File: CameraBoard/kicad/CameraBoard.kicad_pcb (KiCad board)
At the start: 2 copper layers, 101.6 x 76.2 mm, 100 parts, among them Q1 SI7465DP-T1-E3, Q2 BVSS123LT1G, Q3 BSS84, U1 MP26124GR-Z, U2 TPS63070, U3 LM2678SD-12/NOPB, U4 TS5A3159ADBVR, U5 ICM7242IBAZ-SMD, U6 H11F1SR2M, U7 H11F1SR2M, U8 SN74LVC1G17DCKR

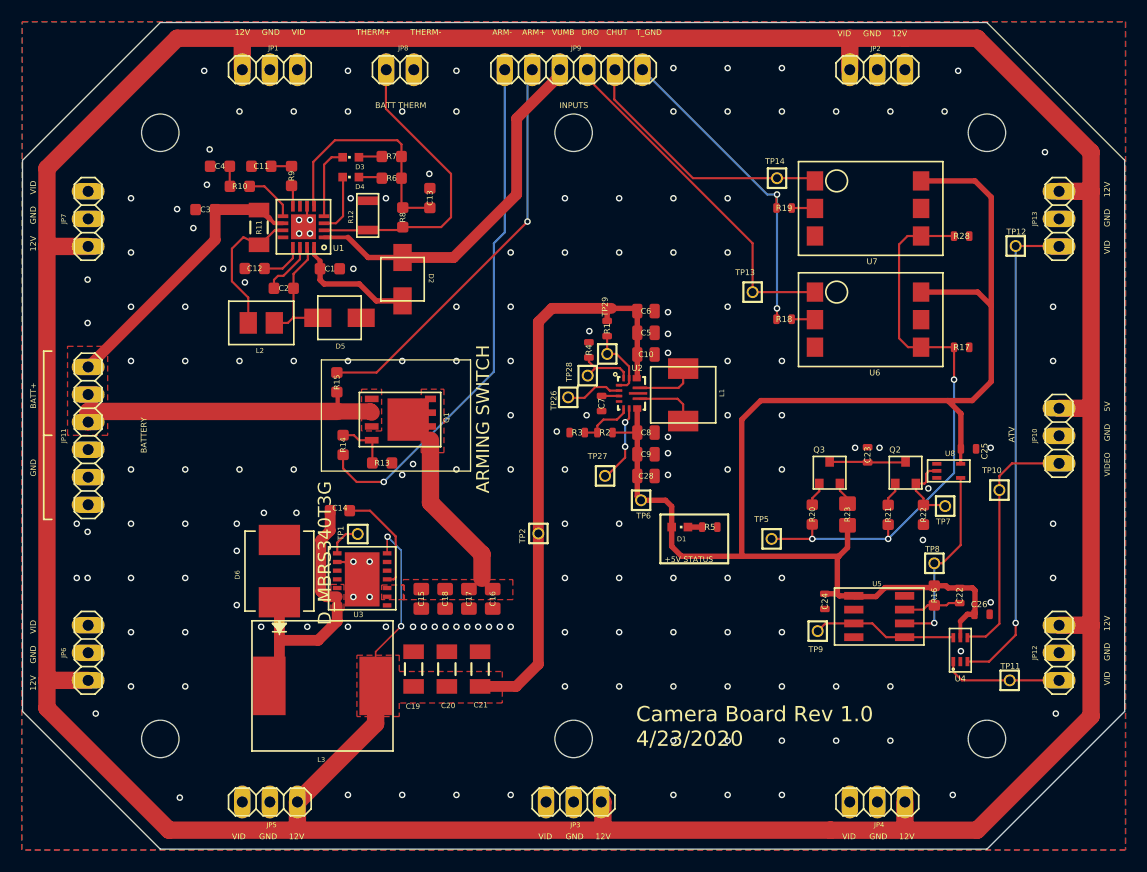
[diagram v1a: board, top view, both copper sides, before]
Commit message: PCB made from new schematic
Made the PCB. There are a few weird errors.
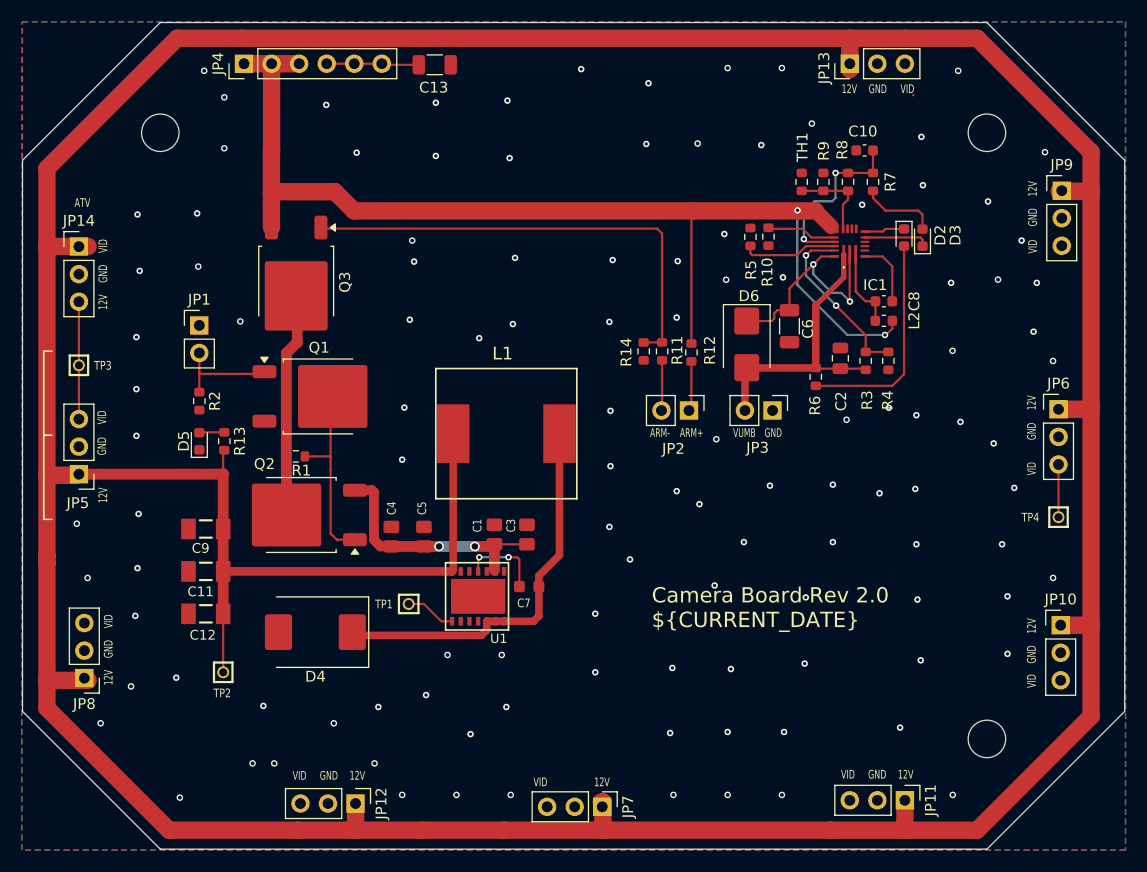
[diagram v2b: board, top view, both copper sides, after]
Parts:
- removed C14: 10n, CameraBoard:.0603-A-NOSILK
- removed C15, C16, C17, C18: 10u, CameraBoard:.0805-B-NOSILK
- removed C19, C20, C21: 47u, CameraBoard:1206-A
- removed C22: 1u, CameraBoard:.0603-C-NOSILK
- removed C23: 20u, CameraBoard:.0603-C-NOSILK
- removed C24, C25, C26: 100n, CameraBoard:.0603-C-NOSILK
- removed C28: 22u, CameraBoard:.0805-C-NOSILK
- removed D1: GRN, CameraBoard:CHIPLED_0603_259
- removed L3: 784770220, CameraBoard:784770220
- removed R15, R22: 1k, CameraBoard:.0603-A-NOSILK
- removed R16: 237k, CameraBoard:.0603-A-NOSILK
- removed R17, R28: 10k, CameraBoard:.0603-C-NOSILK
- removed R18, R19: 60.4, CameraBoard:.0603-C-NOSILK
- removed R20, R21: 10k, CameraBoard:.0603-A-NOSILK
- removed R23: 10, CameraBoard:.0805-A-NOSILK
- removed TP10, TP11, TP12, TP13, TP14, TP26, TP27, TP28, TP29, TP5, TP6, TP7, TP8, TP9: TEST-POINT, CameraBoard:2MM-TEST-POINT
- removed U2: TPS63070, CameraBoard:TPS63070X
- removed U3: LM2678SD-12/NOPB, CameraBoard:LM2678SD-12_NOPB
- removed U4: TS5A3159ADBVR, CameraBoard:TS5A3159ADBVR
- removed U5: ICM7242IBAZ-SMD, CameraBoard:ICM7242IBAZ-SMD
- removed U6, U7: H11F1SR2M, CameraBoard:H11F1SR2M
- removed U8: SN74LVC1G17DCKR, CameraBoard:SN74LVC1G17DCKR
- added IC1: MP2659GQ-0000-Z, psas-footprints:MP2659GQ0000Z, F.Cu at (173.9, 87.3)
- added JP14: PINHD-1X3, Connector_PinHeader_2.54mm:PinHeader_1x03_P2.54mm_Vertical, F.Cu at (102.9, 87.6)
- added TH1: 10k, Resistor_SMD:R_0603_1608Metric, F.Cu at (169.5, 81.6)
- added TP3: Test-Point, CameraBoard:2MM-TEST-POINT, F.Cu at (102.9, 98.5)
- added TP4: Test-Point, CameraBoard:2MM-TEST-POINT, F.Cu at (193.2, 112.5)
- C1: value 4.7u -> 10u; footprint CameraBoard:.0603-A-NOSILK -> CameraBoard:.0805-B-NOSILK
- C10: value 10u -> 1u; footprint CameraBoard:.0805-C-NOSILK -> Capacitor_SMD:C_0603_1608Metric
- C11: value 2.2n -> 47u; footprint CameraBoard:.0603-A-NOSILK -> CameraBoard:1206-A
- C12: value 100n -> 47u; footprint CameraBoard:.0603-A-NOSILK -> CameraBoard:1206-A
- C13: value 1u -> 10u; footprint CameraBoard:.0603-A-NOSILK -> Capacitor_SMD:C_1206_3216Metric
- C2: value 100n -> 1u; footprint CameraBoard:.0603-A-NOSILK -> Capacitor_SMD:C_0805_2012Metric
- C3: footprint CameraBoard:.0603-A-NOSILK -> CameraBoard:.0805-B-NOSILK
- C4: value 4.7n -> 10u; footprint CameraBoard:.0603-A-NOSILK -> CameraBoard:.0805-B-NOSILK
- C5: footprint CameraBoard:.0805-C-NOSILK -> CameraBoard:.0805-B-NOSILK
- C6: value 10u -> 2.2u; footprint CameraBoard:.0805-C-NOSILK -> Capacitor_SMD:C_1206_3216Metric
- C7: value 100n -> 10n; footprint CameraBoard:.0603-C-NOSILK -> CameraBoard:.0603-A-NOSILK
- C8: value 22u -> 100n; footprint CameraBoard:.0805-C-NOSILK -> Capacitor_SMD:C_0603_1608Metric
- C9: value 22u -> 47u; footprint CameraBoard:.0805-C-NOSILK -> CameraBoard:1206-A
- D2, D5: value S2MA-13-F -> LED_Small_Filled; footprint CameraBoard:S2MA-13-F -> LED_SMD:LED_0603_1608Metric
- D3: value SML-D12U1WT86 -> LED_Small_Filled; footprint CameraBoard:CHIPLED_0603_259 -> LED_SMD:LED_0603_1608Metric
- D4: value SML-D12U1WT86 -> D_MBRS340T3G; footprint CameraBoard:CHIPLED_0603_259 -> Diode_SMD:D_SMC
- D6: value D_MBRS340T3G -> B240; footprint CameraBoard:SMC -> Diode_SMD:D_SMB
- JP1, JP2, JP3: value PINHD-1X3 -> ~; footprint CameraBoard:1X03_325 -> Connector_PinHeader_2.54mm:PinHeader_1x02_P2.54mm_Vertical
- JP10, JP12, JP13, JP5, JP6, JP7: footprint CameraBoard:1X03_325 -> Connector_PinHeader_2.54mm:PinHeader_1x03_P2.54mm_Vertical
- JP11, JP9: value PINHD-1X6 -> PINHD-1X3; footprint CameraBoard:1X06_325 -> Connector_PinHeader_2.54mm:PinHeader_1x03_P2.54mm_Vertical
- JP4: value PINHD-1X3 -> PINHD-1X6; footprint CameraBoard:1X03_325 -> Connector_PinHeader_2.54mm:PinHeader_1x06_P2.54mm_Vertical
- JP8: value PINHD-1X2 -> PINHD-1X3; footprint CameraBoard:1X02_325 -> Connector_PinHeader_2.54mm:PinHeader_1x03_P2.54mm_Vertical
- L1: value 1.5uH -> 784770220; footprint CameraBoard:IHLP2020CZER1R5M11 -> CameraBoard:784770220
- L2: value 10uH -> 10uh; footprint CameraBoard:1239AS-H-100M=P2 -> Inductor_SMD:L_0603_1608Metric
- Q1: value SI7465DP-T1-E3 -> SUD08P06-155L; footprint CameraBoard:SI7465DP-T1-E3CT-ND -> Package_TO_SOT_SMD:TO-252-2
- Q2: value BVSS123LT1G -> SUD08P06-155L; footprint CameraBoard:BVSS123LT1G -> Package_TO_SOT_SMD:TO-252-2
- Q3: value BSS84 -> SUD08P06-155L; footprint CameraBoard:BSS84 -> Package_TO_SOT_SMD:TO-252-2
- R1, R4: footprint CameraBoard:.0603-C-NOSILK -> Resistor_SMD:R_0603_1608Metric
- R10: value 750 -> 38.4k; footprint CameraBoard:.0603-A-NOSILK -> Resistor_SMD:R_0603_1608Metric
- R11: value 200m -> 1k; footprint CameraBoard:1206-A -> Resistor_SMD:R_0603_1608Metric
- R12: value 10K -> 1k; footprint CameraBoard:NHQ103B375T10 -> Resistor_SMD:R_0603_1608Metric
- R13: value 150k -> 3.3k; footprint CameraBoard:.0603-A-NOSILK -> Resistor_SMD:R_0603_1608Metric
- R14: value 1k -> 150k; footprint CameraBoard:.0603-A-NOSILK -> Resistor_SMD:R_0603_1608Metric
- R2: value 680k -> 10k; footprint CameraBoard:.0603-C-NOSILK -> Resistor_SMD:R_0603_1608Metric
- R3: value 130k -> 133k; footprint CameraBoard:.0603-C-NOSILK -> Resistor_SMD:R_0603_1608Metric
- R5: value 400 -> 33k; footprint CameraBoard:.0603-C-NOSILK -> Resistor_SMD:R_0603_1608Metric
- R6: value 230 -> 10k; footprint CameraBoard:.0603-A-NOSILK -> Resistor_SMD:R_0603_1608Metric
- R7: value 230 -> 2k; footprint CameraBoard:.0603-A-NOSILK -> Resistor_SMD:R_0603_1608Metric
- R8: value 10k -> 2.26k; footprint CameraBoard:.0603-A-NOSILK -> Resistor_SMD:R_0603_1608Metric
- R9: value 42.5k -> 6.95k; footprint CameraBoard:.0603-A-NOSILK -> Resistor_SMD:R_0603_1608Metric
- TP1, TP2: value TEST-POINT -> Test-Point
- U1: value MP26124GR-Z -> LM2678SD-12/NOPB; footprint CameraBoard:MP26124GR-Z -> CameraBoard:LM2678SD-12_NOPB
- moved JP6 92.2 mm to (193.2, 102.6), turned to 0 degrees
- moved JP4 89.7 mm to (118.1, 70.7), turned to 90 degrees
- moved JP11 82.4 mm to (179.0, 138.6)
- moved JP7 72.0 mm to (151.1, 139.2), turned to -90 degrees
- moved JP12 66.3 mm to (128.4, 138.9)
- moved JP8 63.2 mm to (103.4, 127.3), turned to 180 degrees
- moved L2 57.4 mm to (177.1, 94.4), turned to 0 degrees
- moved Q2 55.9 mm to (123.3, 112.3), turned to 180 degrees
- moved D3 53.2 mm to (180.7, 86.7)
- moved Q3 52.6 mm to (122.9, 90.8), turned to -90 degrees
- moved C2 51.7 mm to (173.1, 97.9), turned to 90 degrees
- moved R9 49.0 mm to (171.5, 81.6)
- moved R10 48.9 mm to (166.5, 86.6), turned to -90 degrees
- moved D6 47.9 mm to (164.5, 96.6), turned to -90 degrees
- moved D2 46.4 mm to (179.0, 86.7)
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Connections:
- C1 pad 1: Net-(D2--) -> Net-(Q2-S)
- C10 pad 1: +12V -> VCC
- C11 pad 1: Net-(C11-Pad1) -> +12V
- C12 pad 1: Net-(C12-Pad1) -> +12V
- C13 pad 1: Net-(C13-Pad1) -> Net-(JP4-Pin_4)
- C2 pad 1: Net-(D5--) -> /VUMB
- C2 pad 2: Net-(C2-Pad2) -> GND
- C3 pad 1: /CameraBoard_1/BATT+ -> Net-(Q2-S)
- C4 pad 1: Net-(C4-Pad1) -> Net-(Q2-S)
- C5 pad 1: +12V -> Net-(Q2-S)
- C6 pad 1: +12V -> GND
- C6 pad 2: GND -> Net-(D6-K)
- C7 pad 1: Net-(U2-VAUX) -> /SOUT
- C7 pad 2: GND -> Net-(U1-CB)
- C8 pad 1: +5V -> Net-(IC1-BST)
- C8 pad 2: GND -> Net-(IC1-SW)
- C9 pad 1: +5V -> +12V
- D6 pad 1: /CameraBoard_1/SOUT -> Net-(D6-K)
- D6 pad 2: GND -> /VUMB
- JP1 pad 1: +12V -> GND
- JP1 pad 2: GND -> Net-(JP1-Pin_2)
- JP10 pad 3: Net-(U4-COM) -> unconnected-(JP10-Pin_3-Pad3)
- JP11 pad 1: /CameraBoard_1/BATT+ -> +12V
- JP11 pad 2: /CameraBoard_1/BATT+ -> GND
- JP11 pad 3: /CameraBoard_1/BATT+ -> unconnected-(JP11-Pin_3-Pad3)
- JP12 pad 3: /CameraBoard_2/CAM_DOWN -> unconnected-(JP12-Pin_3-Pad3)
- JP13 pad 3: /CameraBoard_2/CAM_UP -> unconnected-(JP13-Pin_3-Pad3)
- JP2 pad 1: +12V -> /ARM-OUT
- JP2 pad 2: GND -> /ARM-IN
- JP3 pad 1: +12V -> GND
- JP3 pad 2: GND -> /VUMB
- JP4 pad 1: +12V -> /BATT+
- JP4 pad 2: GND -> /BATT+
- JP4 pad 3: unconnected-(JP4-Pad3) -> /BATT+
- JP5 pad 3: unconnected-(JP5-Pad3) -> /CAM_DOWN
- JP6 pad 3: unconnected-(JP6-Pad3) -> /CAM_UP
- JP8 pad 1: Net-(R12-P$1) -> +12V
- JP9 pad 1: T_GND -> +12V
- JP9 pad 2: CHUTE -> GND
- JP9 pad 3: DROGUE -> unconnected-(JP9-Pin_3-Pad3)
- Q2 pad 1: Net-(Q2-G) -> Net-(Q1-D)
- Q2 pad 2: Net-(Q2-S) -> VBATT
- Q2 pad 3: Net-(Q2-D) -> Net-(Q2-S)
- Q3 pad 2: Net-(Q3-S) -> VBATT
- Q3 pad 3: Net-(Q2-D) -> /BATT+
- R1 pad 1: Net-(U2-EN) -> VBATT
- R1 pad 2: +12V -> Net-(Q1-D)
- R10 pad 1: Net-(R10-Pad1) -> Net-(IC1-ISET)
- R10 pad 2: Net-(C4-Pad1) -> GND
- R11 pad 1: Net-(L2-P$2) -> /ARM-IN
- R11 pad 2: /CameraBoard_1/BATT+ -> Net-(Q3-G)
- R13 pad 1: GND -> Net-(D5-A)
- R13 pad 2: Net-(Q1-PadG) -> +12V
- R14 pad 1: Net-(Q1-PadG) -> Net-(Q3-G)
- R14 pad 2: /CameraBoard_1/ARM-IN -> GND
- R2 pad 1: Net-(U2-FB) -> Net-(JP1-Pin_2)
- R2 pad 2: +5V -> GND
- R3 pad 1: GND -> Net-(IC1-VDPM)
- R3 pad 2: Net-(U2-FB) -> /VUMB
- R4 pad 2: Net-(U2-VSEL) -> Net-(IC1-VDPM)
- R6 pad 1: Net-(D4-PadA) -> /VUMB
- R6 pad 2: Net-(C13-Pad1) -> Net-(D2-A)
- R7 pad 1: Net-(D3-PadA) -> VCC
- R7 pad 2: Net-(C13-Pad1) -> Net-(D3-A)
- R8 pad 1: Net-(R12-P$1) -> VCC
- R8 pad 2: Net-(C13-Pad1) -> Net-(IC1-NTC)
- R9 pad 1: Net-(R9-Pad1) -> Net-(IC1-NTC)
- R9 pad 2: Net-(C11-Pad1) -> GND
- TP1 pad 1: Net-(U3-ON) -> Net-(U1-ON)
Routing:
- net +5V: track 134.4 -> 0.00 mm
- net /BATT+: track 0.00 -> 103.8 mm, vias 0 -> 2
- net /CameraBoard_1/BATT+: track 55.1 -> 0.00 mm
- net /CameraBoard_2/TIMERPULSE: track 53.0 -> 0.00 mm, vias 3 -> 0
- net /CameraBoard_1/ARM-IN: track 48.1 -> 0.00 mm, vias 1 -> 0
- net /CameraBoard_2/CAM_UP: track 45.3 -> 0.00 mm, vias 1 -> 0
- net Net-(Q3-G): track 2.22 -> 43.4 mm
- net /CameraBoard_1/ARM-OUT: track 37.5 -> 0.00 mm, vias 1 -> 0
- net /SOUT: track 0.00 -> 36.1 mm
- net /CameraBoard_1/VUMB: track 34.1 -> 0.00 mm
- net DROGUE: track 32.6 -> 0.00 mm
- net T_GND: track 30.0 -> 0.00 mm, vias 2 -> 0
- net Net-(R12-P$1): track 28.3 -> 0.00 mm
- net /VUMB: track 0.00 -> 26.2 mm
- net /CameraBoard_1/SOUT: track 25.1 -> 0.00 mm
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- removed copper zone on F.Cu, net +12V
- removed copper zone on F.Cu, net +16V
- removed copper zone on F.Cu, net /CameraBoard_1/BATT+
- removed copper zone on F.Cu, net /CameraBoard_1/SOUT
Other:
- outline, holes or cut-outs redrawn
- board text added: "Camera Board Rev 2.0 ${CURRENT_DATE}"
- board text removed: "+5V STATUS"
- board text removed: "12V SPS"
- board text removed: "5V"
- board text removed: "5V SPS"
- board text removed: "ARMING SWITCH"
- board text removed: "BATT THERM"
- board text removed: "BATT+"
- board text removed: "BATTERY"
- board text removed: "CHUT"
- board text removed: "Camera Board Rev 1.0 4/23/2020"
- board text removed: "DRO"
- board text removed: "INPUTS"
- board text removed: "Inputs"
- board text removed: "LiPo Charger"
- board text removed: "Pulse Generator"
- board text removed: "THERM+"
- board text removed: "THERM-"
- board text removed: "T_GND"
- board text removed: "Timer"
- board text removed: "VIDEO"

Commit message: Updates to PCB
Track width changes
Fixed silkscreens
changed ground zone settings
Added IC Batt zone
Dropped test points for cams
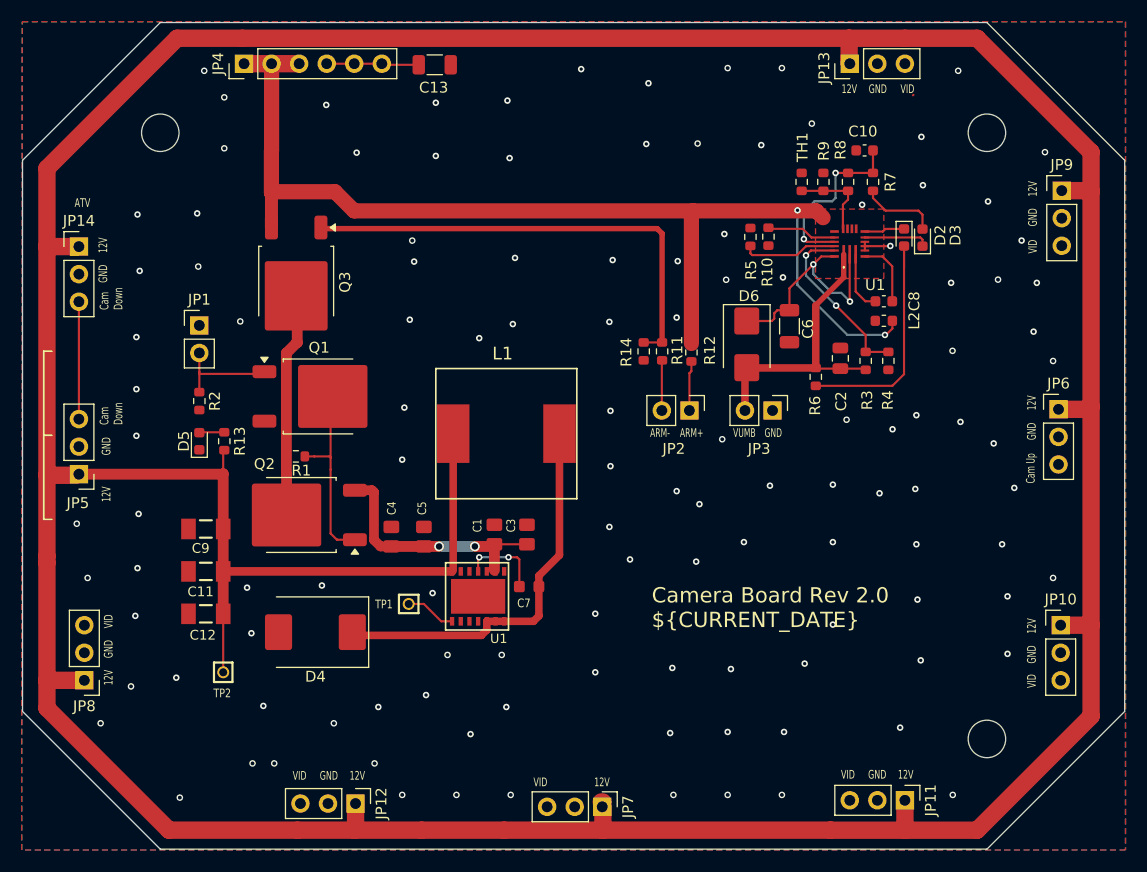
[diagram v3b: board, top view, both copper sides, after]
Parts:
- removed TP3, TP4: Test-Point, CameraBoard:2MM-TEST-POINT
- moved JP8 0.20 mm to (103.4, 127.5)
- renumbered IC1 to U1
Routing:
- net /CAM_UP: track 4.86 -> 0.00 mm
- net GND: track 0.18 -> 3.34 mm, vias 117 -> 122
- net +12V: track 410.3 -> 408.0 mm
- net Net-(IC1-SW): track 7.56 -> 5.63 mm
- net /BATT+: track 103.8 -> 102.7 mm
- net /ARM-IN: track 4.10 -> 4.64 mm
- net /ARM-OUT: track 4.07 -> 4.60 mm
- added copper zone on F.Cu, net /BATT+
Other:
- board text added: "Cam Down"
- board text added: "Cam Up"
